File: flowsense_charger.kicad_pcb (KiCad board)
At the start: 2 copper layers, 39.6 x 27.5 mm, 39 parts, among them J1 SOLAR, J2 LOAD, J3 Conn_01x02_Pin, J4 LOAD, J5 USB_A, J6 Conn_01x02_Pin, J7 SOLAR, J8 Conn_01x02_Pin, J9 Conn_01x02_Pin, SW1 SW_Push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

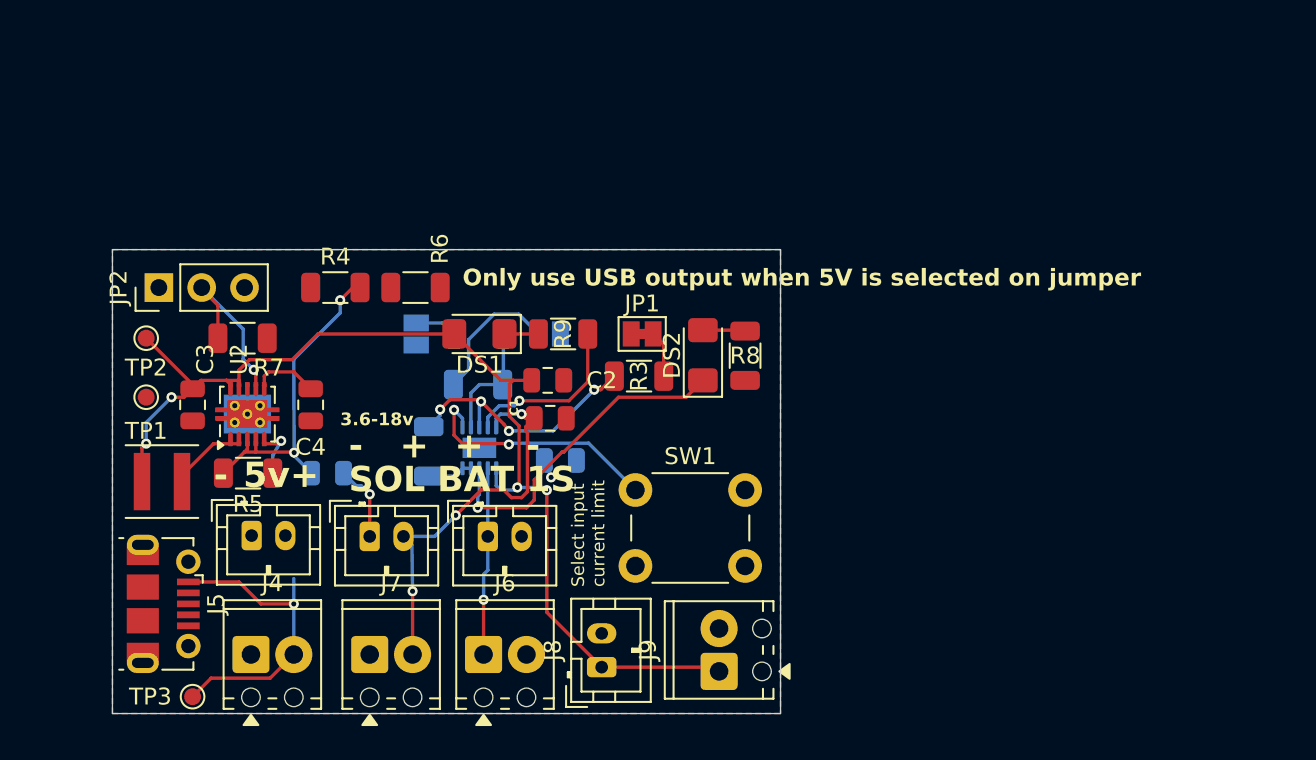
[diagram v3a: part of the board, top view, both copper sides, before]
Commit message: Layout all components on a single face for easier manufacturing
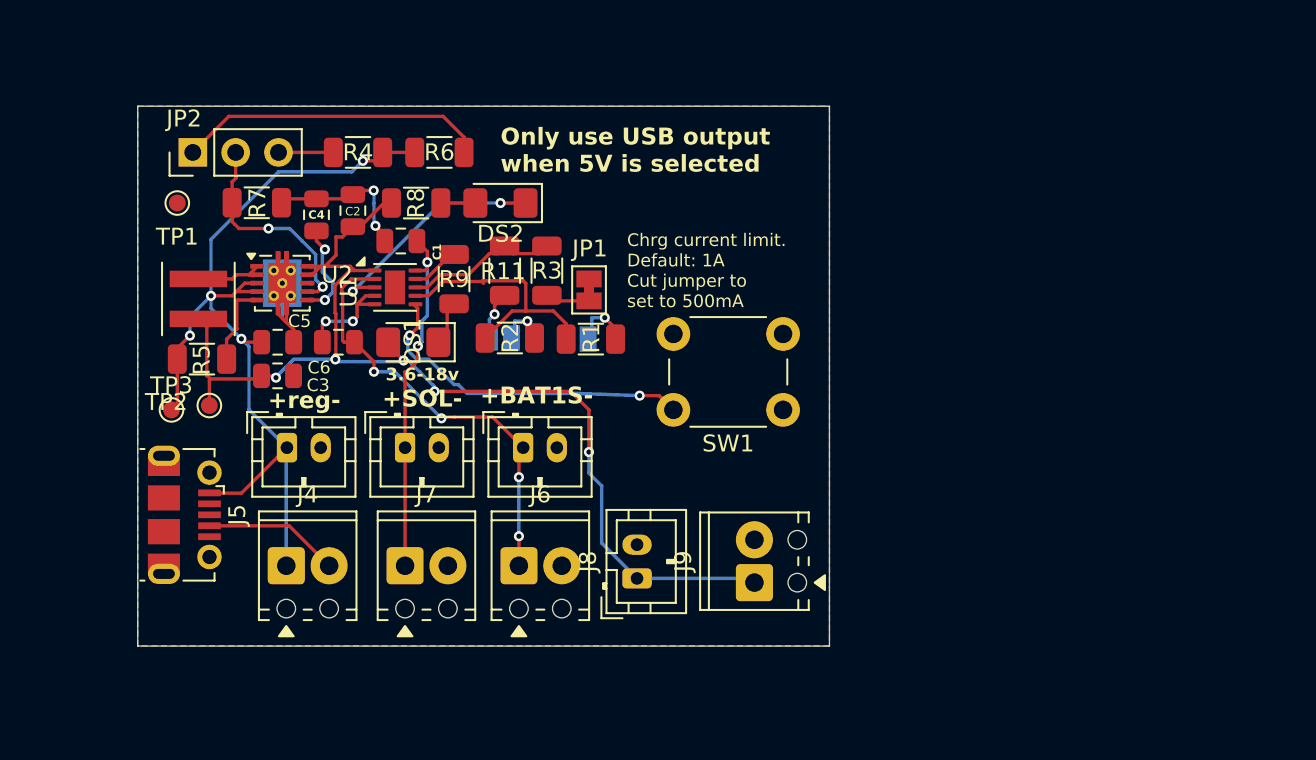
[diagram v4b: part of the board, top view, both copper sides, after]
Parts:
- C5, C6, R1, R11, R2, U1: moved to F.Cu
- moved R8 21.5 mm to (43.5, 67.7), turned to 180 degrees
- moved TP3 17.0 mm to (29.0, 80.0), turned to 0 degrees
- moved C2 15.3 mm to (39.8, 68.2), turned to 90 degrees
- moved DS2 15.0 mm to (48.5, 67.7), turned to 180 degrees
- moved C6 14.9 mm to (38.9, 76.0), turned to 0 degrees
- moved C1 13.7 mm to (42.6, 70.0), turned to 180 degrees
- moved TP1 11.7 mm to (29.3, 67.7)
- moved R11 11.6 mm to (48.8, 71.8)
- moved C4 11.3 mm to (37.6, 68.4), turned to 90 degrees
- moved L1-XFL4020-102MEB1 11.0 mm to (30.6, 73.4), turned to 90 degrees
- moved U1 10.7 mm to (42.2, 72.7), turned to 0 degrees
- moved SW1 9.96 mm to (65.2, 80.0), turned to 180 degrees
- moved C5 8.30 mm to (35.3, 76.0)
- moved R3 8.30 mm to (51.2, 71.8), turned to -90 degrees
- moved JP2 8.26 mm to (30.3, 64.7)
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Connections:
- C1 pad 1: Net-(J1-Pin_2) -> Net-(J1-Pin_1)
- J1 pad 1: GND -> Net-(J1-Pin_1)
- J1 pad 2: Net-(J1-Pin_2) -> GND
- J2 pad 1: GND -> VCC
- J2 pad 2: VCC -> GND
- J4 pad 1: GND -> VCC
- J4 pad 2: VCC -> GND
- J5 pad 1: VOUT -> VCC
- J7 pad 1: GND -> Net-(J1-Pin_1)
- J7 pad 2: Net-(J1-Pin_2) -> GND
- TP3 pad 1: +5V -> VCC
- U1 pad 10: Net-(J1-Pin_2) -> Net-(J1-Pin_1)
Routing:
- net VCC: track 19.3 -> 54.2 mm, vias 2 -> 4
- net GND: track 6.86 -> 31.9 mm, vias 1 -> 5
- net Net-(J1-Pin_2): track 23.6 -> 0.00 mm, vias 3 -> 0
- net Net-(J1-Pin_1): track 0.00 -> 21.7 mm, vias 0 -> 2
- net Net-(JP2-A): track 0.00 -> 18.4 mm
- net +5V: track 18.3 -> 0.00 mm, vias 1 -> 0
- net +BATT: track 11.6 -> 26.4 mm, vias 2 -> 4
- net ILIM: track 7.15 -> 15.7 mm
- net Net-(U1-STAT1): track 10.2 -> 2.89 mm, vias 1 -> 0
- net ISET: track 15.6 -> 9.18 mm, vias 4 -> 0
- net Net-(DS2-K): track 19.6 -> 13.8 mm, vias 1 -> 2
- net Net-(U1-TS/MR): track 14.9 -> 20.2 mm
- net Net-(JP1_1100mA_4.2v1-B): track 8.29 -> 3.66 mm, vias 0 -> 1
- net Net-(JP2-B): track 0.00 -> 3.25 mm
- net SET_V: track 10.5 -> 13.2 mm, vias 1 -> 2
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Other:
- board size 39.6 x 27.5 mm -> 41 x 32 mm
- board text added: "+BAT1S-"
- board text added: "+SOL-"
- board text added: "+reg-"
- board text added: "Chrg current limit. Default: 1A Cut jumper to set to 500mA"
- board text added: "Only use USB output when 5V is selected"
- board text removed: "+"
- board text removed: "-"
- board text removed: "5v"
- board text removed: "BAT 1S"
- board text removed: "Only use USB output when 5V is selected on jumper"
- board text removed: "SOL"
- board text removed: "Select input current limit"

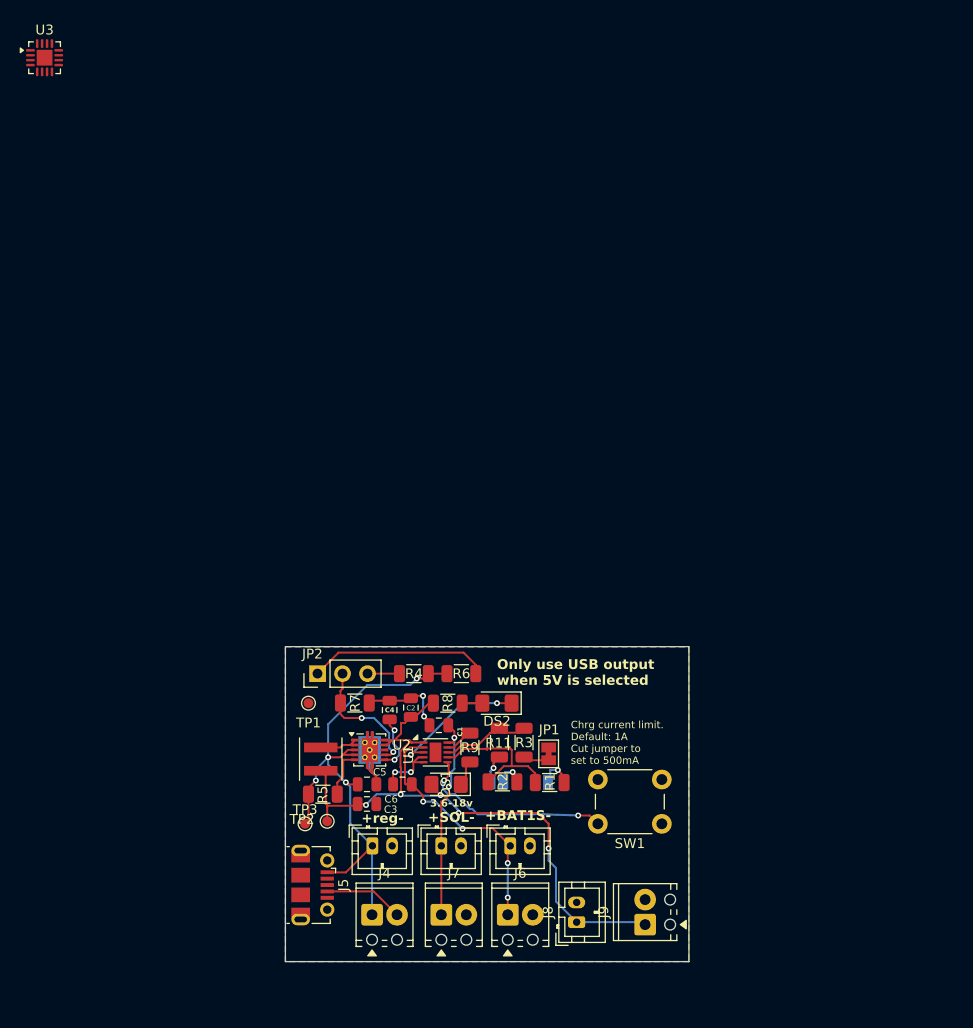
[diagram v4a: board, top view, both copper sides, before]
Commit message: Removes old design file. Updates current file with design that passes DRC.
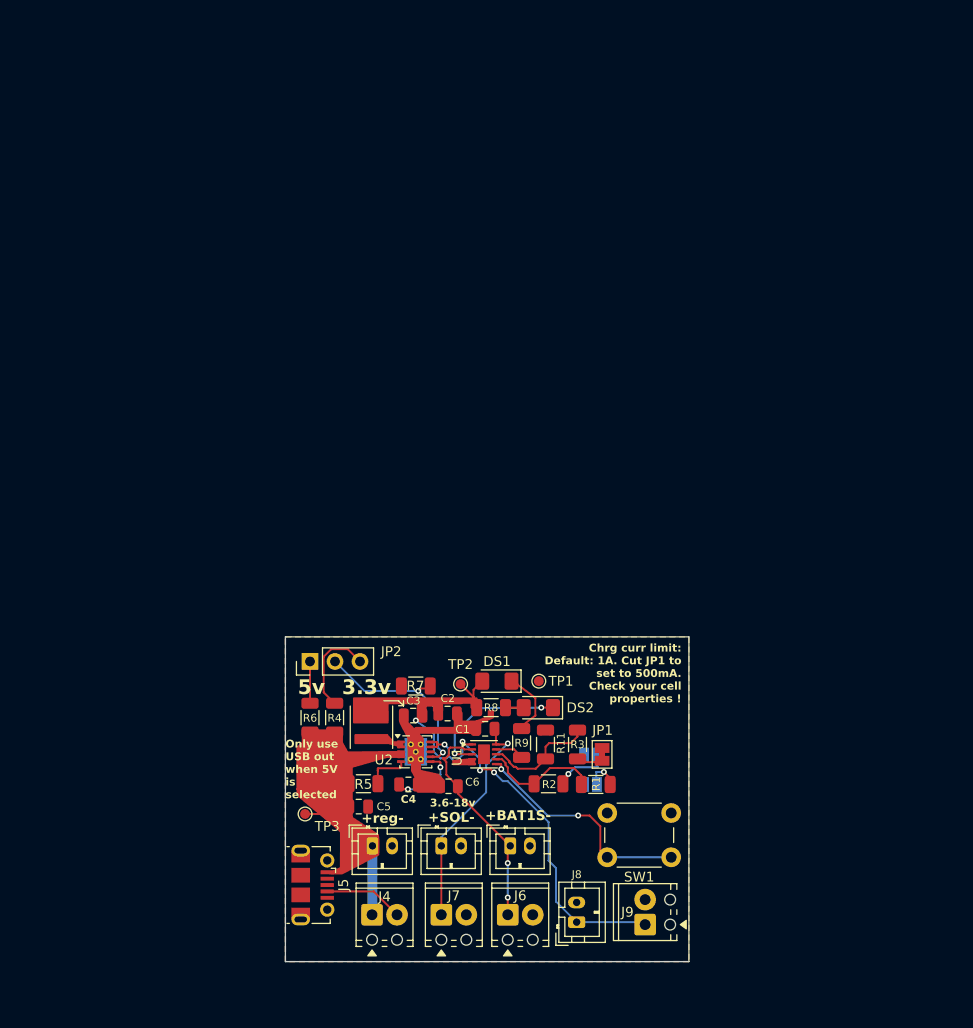
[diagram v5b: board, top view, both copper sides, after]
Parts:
- removed JP1_1100mA_4.2v1, JP2_500mA_4.2v1: SolderJumper_2_Open, Jumper:SolderJumper-2_P1.3mm_Open_Pad1.0x1.5mm
- removed U3: BQ24074RGT, Package_DFN_QFN:VQFN-16-1EP_3x3mm_P0.5mm_EP1.6x1.6mm
- added 1100mA_4.2v1: SolderJumper_2_Open, Jumper:SolderJumper-2_P1.3mm_Open_Pad1.0x1.5mm, B.Cu at (58.0, 76.0)
- added 500mA_4.2v1: SolderJumper_2_Open, Jumper:SolderJumper-2_P1.3mm_Open_Pad1.0x1.5mm, B.Cu at (58.0, 73.0)
- moved TP1 23.5 mm to (52.8, 65.5)
- moved TP2 19.4 mm to (44.8, 65.8)
- moved R6 16.0 mm to (29.5, 69.2), turned to 90 degrees
- moved DS1 11.7 mm to (48.5, 65.5)
- moved C3 10.1 mm to (40.0, 69.0), turned to 180 degrees
- moved R4 9.21 mm to (32.0, 69.2), turned to -90 degrees
- moved C4 7.80 mm to (39.5, 76.0), turned to 0 degrees
- moved R7 6.43 mm to (40.2, 66.0), turned to 180 degrees
- moved L1-XFL4020-102MEB1 6.08 mm to (35.7, 70.2), turned to -90 degrees
- moved R3 5.43 mm to (56.7, 71.9)
- moved JP1 5.43 mm to (59.2, 72.9)
- moved R9 5.27 mm to (51.0, 71.8), turned to -90 degrees
- moved U1 4.93 mm to (47.2, 72.9)
- moved C1 4.72 mm to (47.3, 70.3)
- moved C6 4.68 mm to (43.6, 76.2)
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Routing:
- net VCC: track 54.2 -> 3.72 mm, vias 4 -> 0
- net GND: track 31.9 -> 9.64 mm, vias 5 -> 0
- net V_SYS: track 66.6 -> 52.4 mm
- net Net-(JP2-A): track 18.4 -> 4.25 mm
- net Net-(JP2-B): track 3.25 -> 9.72 mm
- net SET_V: track 13.2 -> 19.4 mm
- net Net-(DS1-K): track 2.69 -> 6.80 mm
- net Net-(L1-XFL4020-102MEB1-Pad2): track 4.03 -> 0.00 mm
- net +BATT: track 26.4 -> 22.7 mm, vias 4 -> 2
- net ILIM: track 15.7 -> 12.3 mm
- net Net-(500mA_4.2v1-B): track 3.01 -> 6.30 mm
- net Net-(U1-TS/MR): track 20.2 -> 23.5 mm
- net ISET: track 9.18 -> 11.7 mm
- net Net-(U2-SS): track 5.89 -> 7.93 mm
- net Net-(J1-Pin_1): track 21.7 -> 23.3 mm, vias 2 -> 1
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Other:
- board size 41 x 32 mm -> 41 x 33 mm
- board text added: "3.3v"
- board text added: "5v"
- board text added: "Chrg curr limit: Default: 1A. Cut JP1 to set to 500mA. Check your cell properties !"
- board text added: "Only use USB out when 5V is selected"
- board text added: "Solder gap to set input current limit. Solder at least one Do not solder both. Ensure your cell voltage is compatible with set voltage"
- board text removed: "Chrg current limit. Default: 1A Cut jumper to set to 500mA"
- board text removed: "Only use USB output when 5V is selected"
- board text removed: "Solder gap to set charging current limit Do not solder both. Ensure your cell is compatible with charging current !"

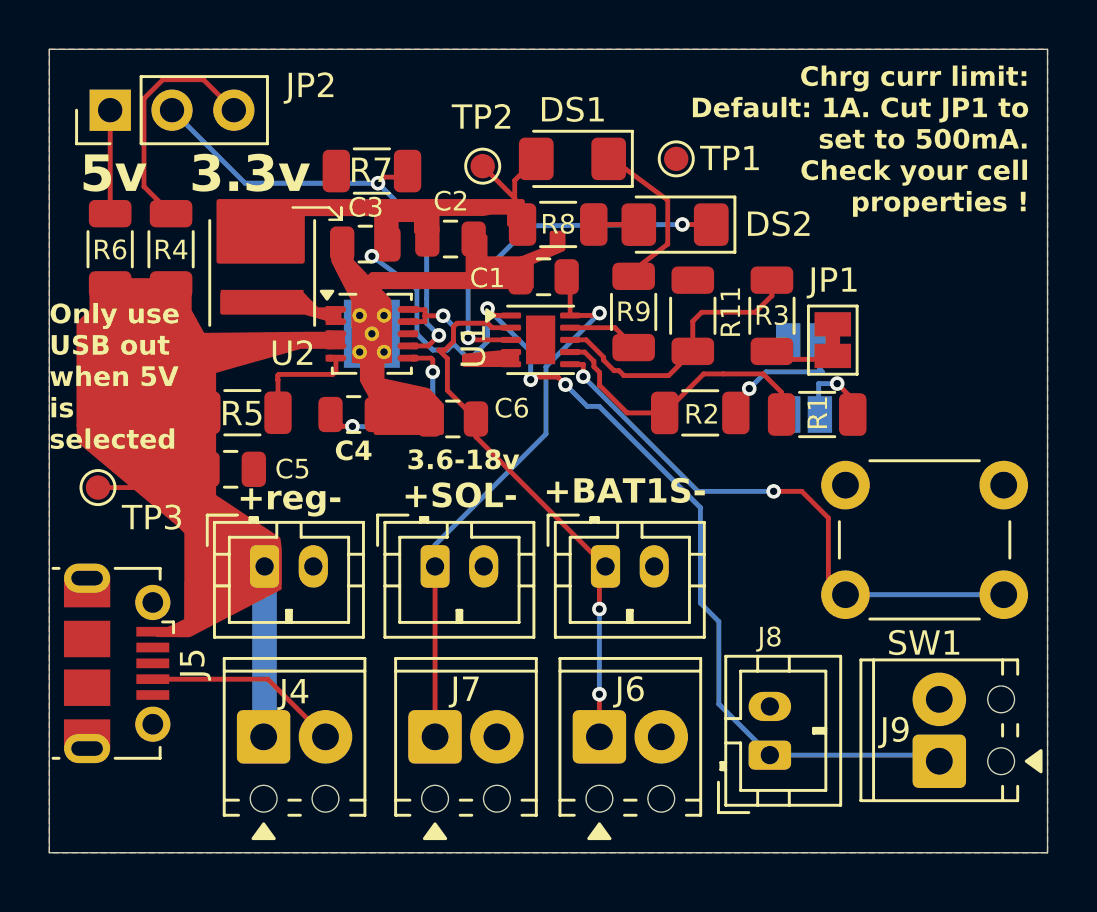
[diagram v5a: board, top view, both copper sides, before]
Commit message: Updates readme with latest info. Updates silkscreen infos. Ignore thermal relief warnings. Champfer board edges
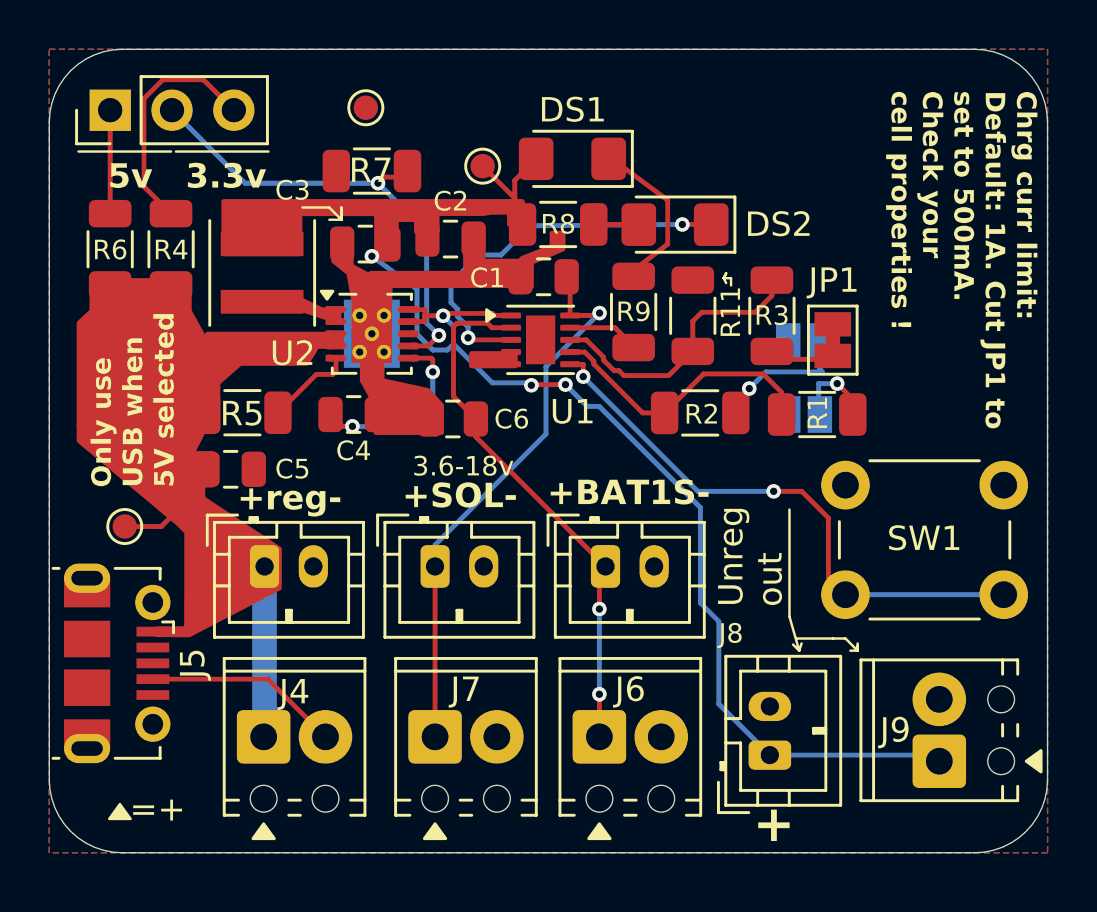
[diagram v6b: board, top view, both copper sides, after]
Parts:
- moved TP1 12.9 mm to (40.0, 63.4)
- moved TP3 1.94 mm to (30.1, 80.6)
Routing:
- net V_SYS: track 52.4 -> 50.7 mm, vias 5 -> 4
- net GND: track 9.64 -> 8.36 mm
- net Net-(DS2-K): track 14.9 -> 16.0 mm
- net VCC: track 3.72 -> 2.71 mm
- net Net-(U2-PG): track 4.54 -> 3.63 mm
- net +BATT: track 22.7 -> 22.0 mm
- net ILIM: track 12.3 -> 11.7 mm
- net Net-(500mA_4.2v1-B): track 6.30 -> 5.80 mm
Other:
- outline, holes or cut-outs redrawn
- board text added: "+"
- board text added: "=+"
- board text added: "Only use USB when 5V selected"
- board text added: "Unreg out"
- board text removed: "Only use USB out when 5V is selected"
